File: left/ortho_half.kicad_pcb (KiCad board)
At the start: 2 copper layers, 150.9 x 146.1 mm, 73 parts, among them J1 AudioJack4, J10 Conn_01x04, J11 Conn_01x01, J12 Conn_01x02, J13 Conn_01x01, J14 Conn_01x01, J15 Conn_01x01, J16 Conn_01x01, J17 Conn_01x01, J2 Conn_01x01, J3 Conn_01x01, J4 Conn_01x01, J5 Conn_01x01, J6 Conn_01x01, J7 Conn_01x01, J8 Conn_01x01, J9 Conn_01x01, K11 KEYSW_RGB, K12 KEYSW_RGB, K13 KEYSW_RGB, K14 KEYSW_RGB, K15 KEYSW_RGB, K16 KEYSW_RGB, K21 KEYSW_RGB, K22 KEYSW_RGB, K23 KEYSW_RGB, K24 KEYSW_RGB, K25 KEYSW_RGB, K26 KEYSW_RGB, K31 KEYSW_RGB, K32 KEYSW_RGB, K33 KEYSW_RGB, K34 KEYSW_RGB, K35 KEYSW_RGB, K36 KEYSW_RGB, K41 KEYSW_RGB, K42 KEYSW_RGB, K43 KEYSW_RGB, K44 KEYSW_RGB, K45 KEYSW_RGB, K46 KEYSW_RGB, K51 KEYSW_RGB, K52 KEYSW_RGB, K53 KEYSW_RGB, K54 KEYSW_RGB, K55 KEYSW_RGB, K56 KEYSW_RGB, K61 KEYSW_RGB, K62 KEYSW_RGB, K63 KEYSW_RGB, K64 KEYSW_RGB, K65 KEYSW_RGB, K66 KEYSW_RGB, SW1 SW_PUSH_RESET, SW2 Rotary_Encoder_Switch, SW4 SW_SPST, SW5 SW_SPST, SW6 SW_SPST, U1 microctrl_superset, U2 IS31FL3733-TQ

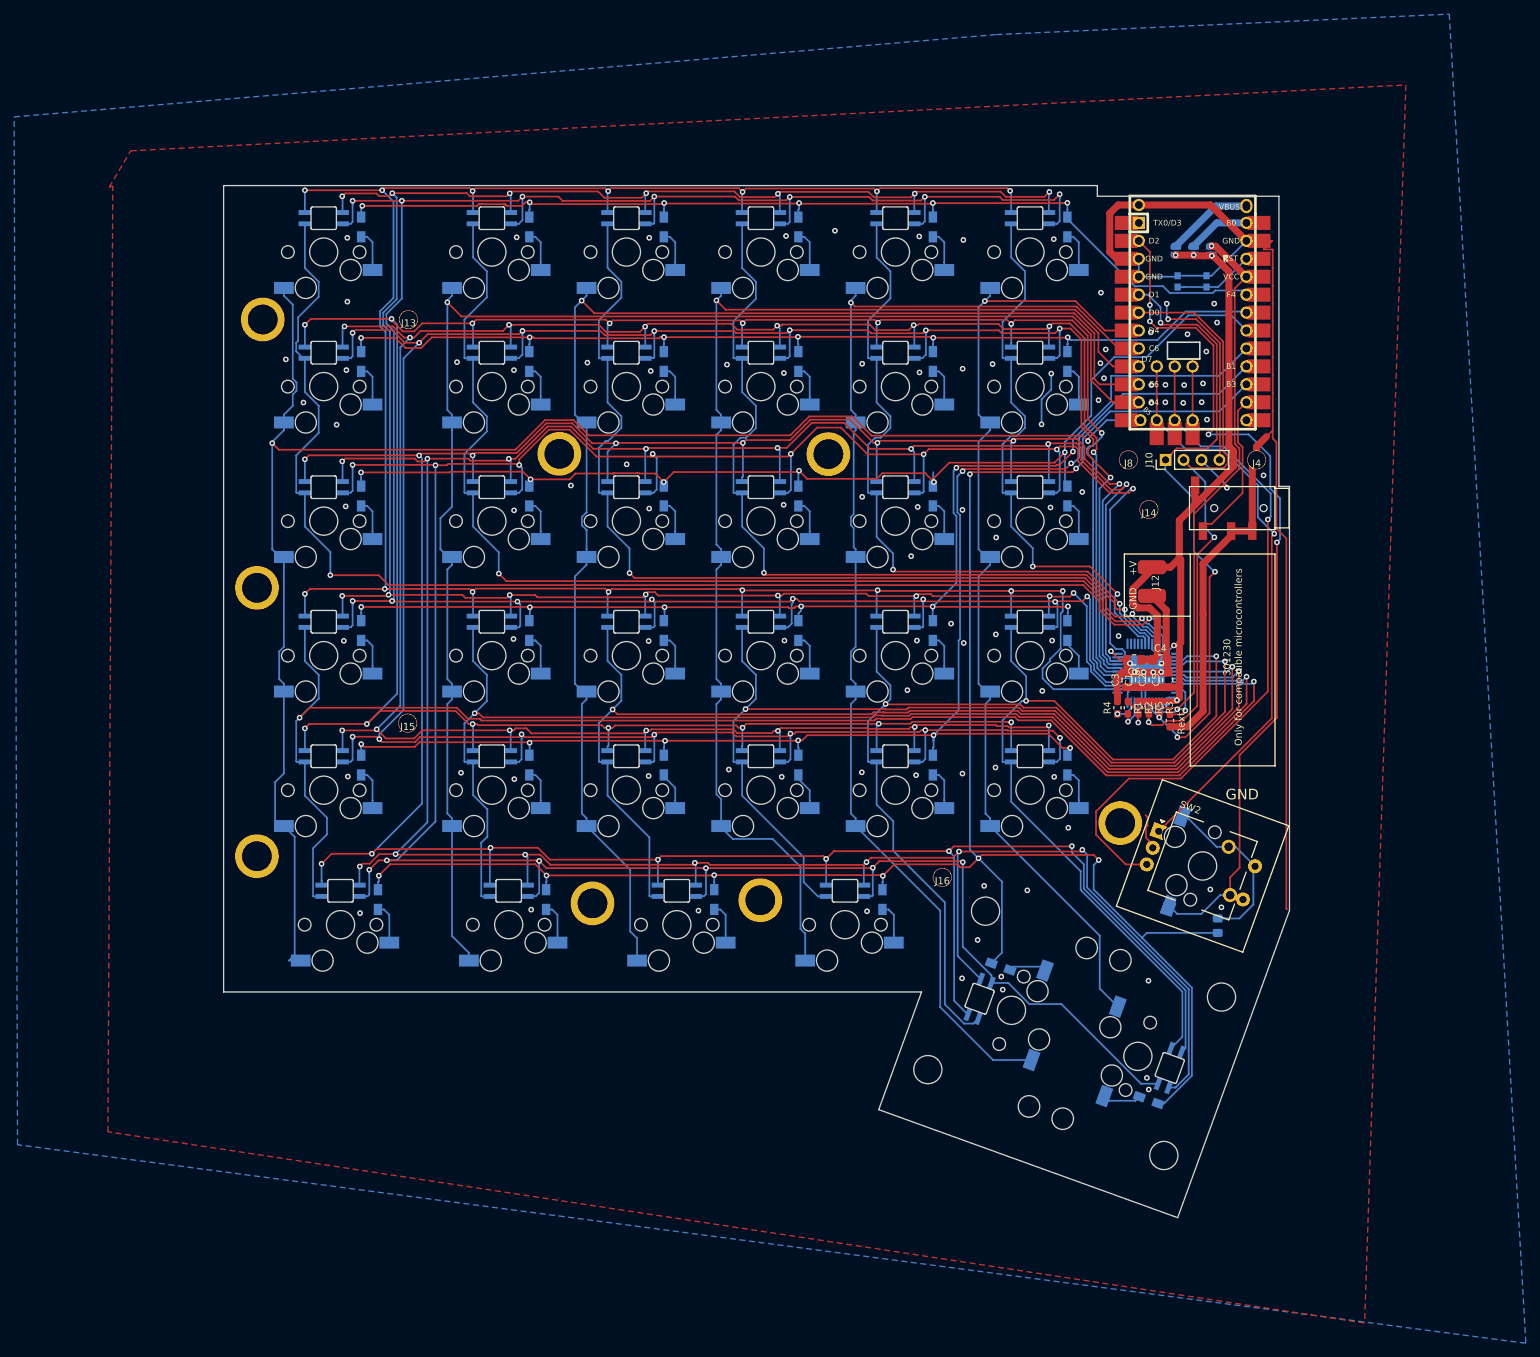
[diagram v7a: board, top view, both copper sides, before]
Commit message: Kicad 6 migration; other fixes
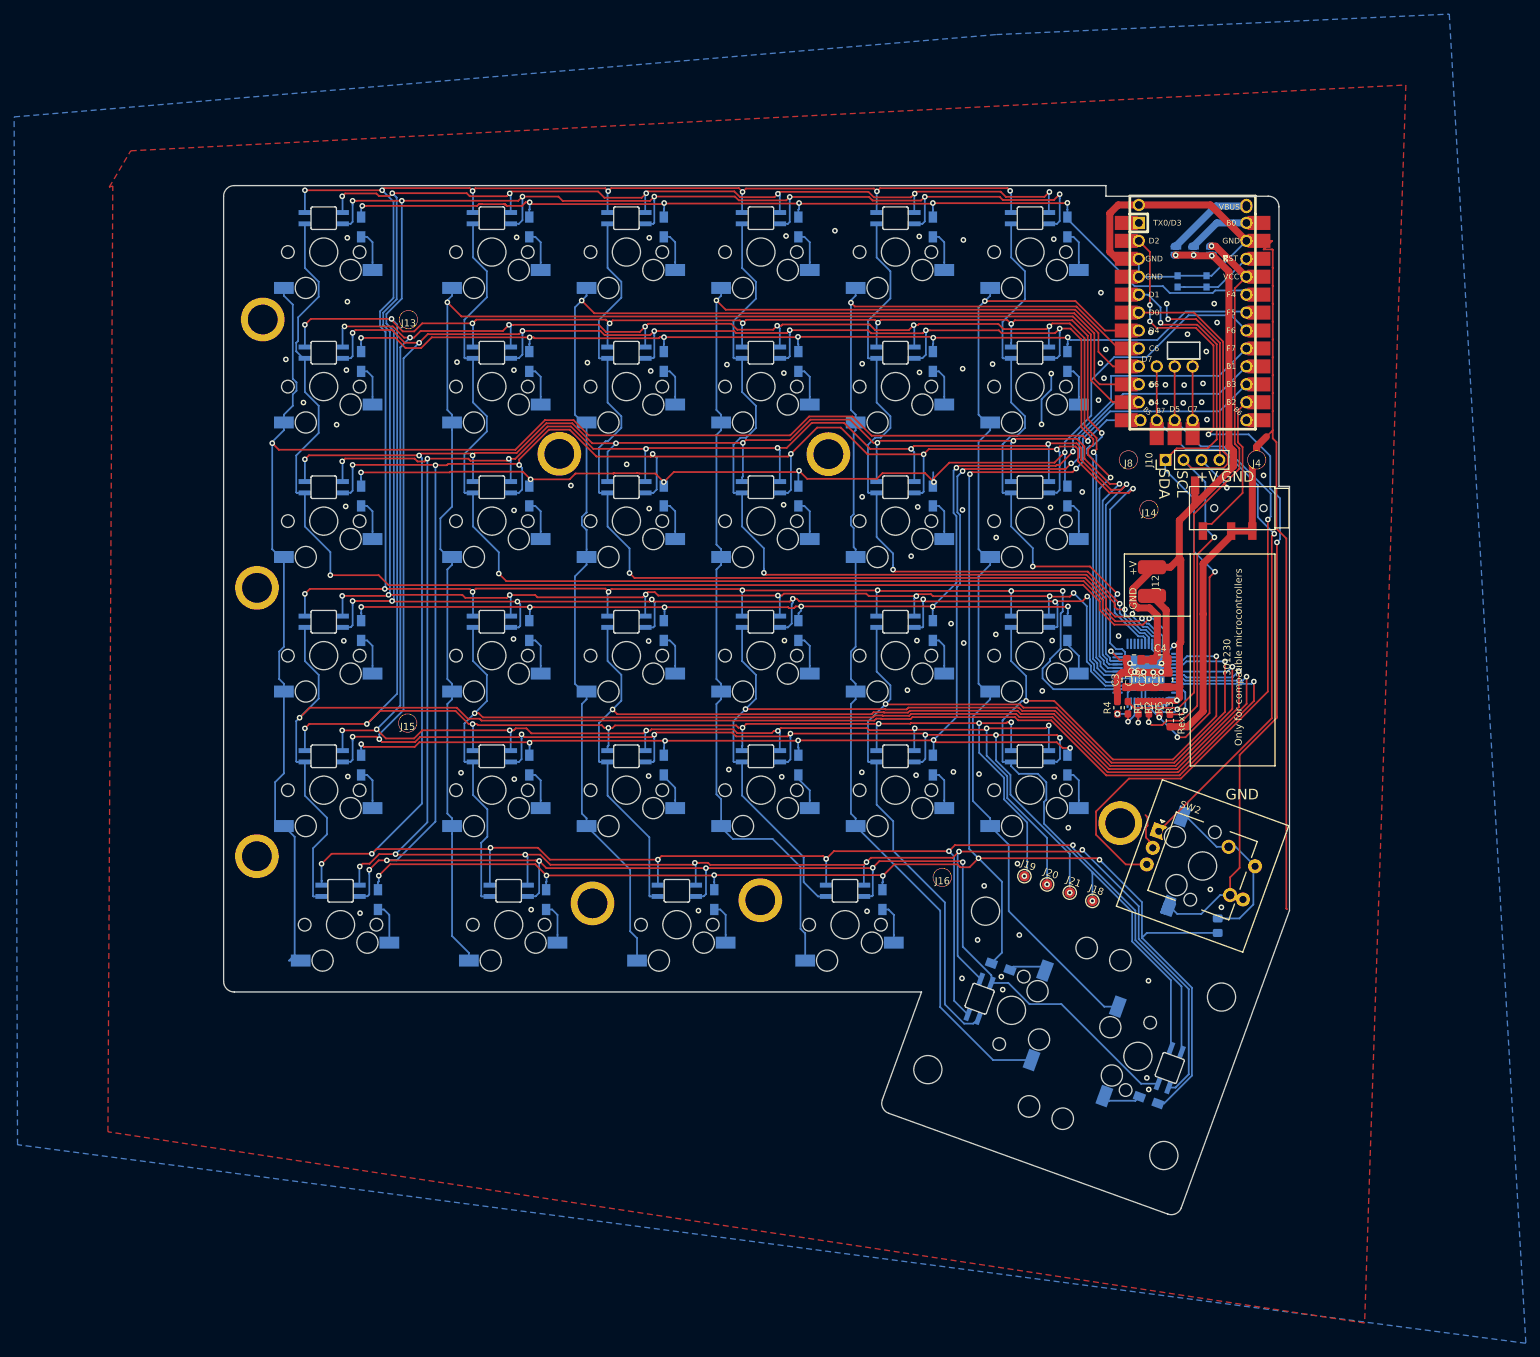
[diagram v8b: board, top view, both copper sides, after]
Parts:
- added J18: Conn_01x01, TestPoint:TestPoint_Pad_D1.5mm, F.Cu at (127.9, 115.7)
- added J19: Conn_01x01, TestPoint:TestPoint_Pad_D1.5mm, F.Cu at (118.3, 112.2)
- added J20: Conn_01x01, TestPoint:TestPoint_Pad_D1.5mm, F.Cu at (121.5, 113.4)
- added J21: Conn_01x01, TestPoint:TestPoint_Pad_D1.5mm, F.Cu at (124.7, 114.5)
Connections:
- J17 pad 1: (no net) -> GND
- K11 pad 5: led_col1 -> unconnected-(K11-Pad5)
- K21 pad 5: led_col1 -> unconnected-(K21-Pad5)
- K41 pad 5: led_col9 -> unconnected-(K41-Pad5)
- K51 pad 5: led_col9 -> unconnected-(K51-Pad5)
- U1 pad 13: Net-(U1-Pad13) -> unconnected-(U1-Pad13)
- U1 pad 27: Net-(U1-Pad27) -> unconnected-(U1-Pad27)
- U2 pad 1: (no net) -> unconnected-(U2-Pad1)
- U2 pad 13: (no net) -> unconnected-(U2-Pad13)
- U2 pad 14: (no net) -> unconnected-(U2-Pad14)
- U2 pad 15: (no net) -> unconnected-(U2-Pad15)
- U2 pad 16: (no net) -> unconnected-(U2-Pad16)
- U2 pad 17: (no net) -> unconnected-(U2-Pad17)
- U2 pad 25: (no net) -> unconnected-(U2-Pad25)
- U2 pad 26: (no net) -> unconnected-(U2-Pad26)
- U2 pad 36: (no net) -> unconnected-(U2-Pad36)
- U2 pad 40: (no net) -> unconnected-(U2-Pad40)
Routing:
- net led_row2B: track 357.7 -> 383.3 mm, vias 15 -> 17
- net led_row2C: track 381.3 -> 406.9 mm, vias 15 -> 17
- net led_row2A: track 371.9 -> 396.5 mm, vias 15 -> 17
- net unconnected-(U1-Pad27): track 0.00 -> 9.52 mm
- net Net-(U1-Pad27): track 9.52 -> 0.00 mm
- net led_col14: track 121.4 -> 126.0 mm, vias 2 -> 3
- net col6: track 138.7 -> 141.3 mm
- net unconnected-(U1-Pad13): track 0.00 -> 1.78 mm
- net Net-(U1-Pad13): track 1.78 -> 0.00 mm
- net row5: track 203.8 -> 202.4 mm
- net row6: track 287.3 -> 286.4 mm
- net GND: vias 106 -> 107
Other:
- board size 150.9 x 146.1 mm -> 150.9 x 145.7 mm
- net class Default removed
- board text added: "+V"
- board text added: "SCL"
- board text added: "SDA"
